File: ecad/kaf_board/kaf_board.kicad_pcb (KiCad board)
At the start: 4 copper layers, 116 x 71 mm, 234 parts, among them J1 Barrel_Jack_Switch, J2 USB_OTG, J3 AUX, J4 Peltier1, J5 Peltier2, M1 Motor_Servo, M2 Servo cut-out, Q1 MMBT3904LT1G, Q2 NTD4804N, Q3 NTD4804N, U1 MAX4649, U10 LM224, U11 LM224, U12 LM224, U13 LD1117S12CTR_SOT223, U14 LD1117S33CTR_SOT223, U15 LTC3265*FE, U16 93LCxxBxxOT, U17 FT2232H, U18 ICE40HX1K-VQ100, U19 W25X20CL, U2 ADP7118AUJZ, U20 MCP3004, U21 TC4427, U3 AD9826, U4 KAF-CDIP24, U5 TL432LIAIDBZR, U6 TL432LIAIDBZR, U7 TC4427, U8 TC4427, U9 TC4428, X1 KC7050A-C3, Y1 12 MHz

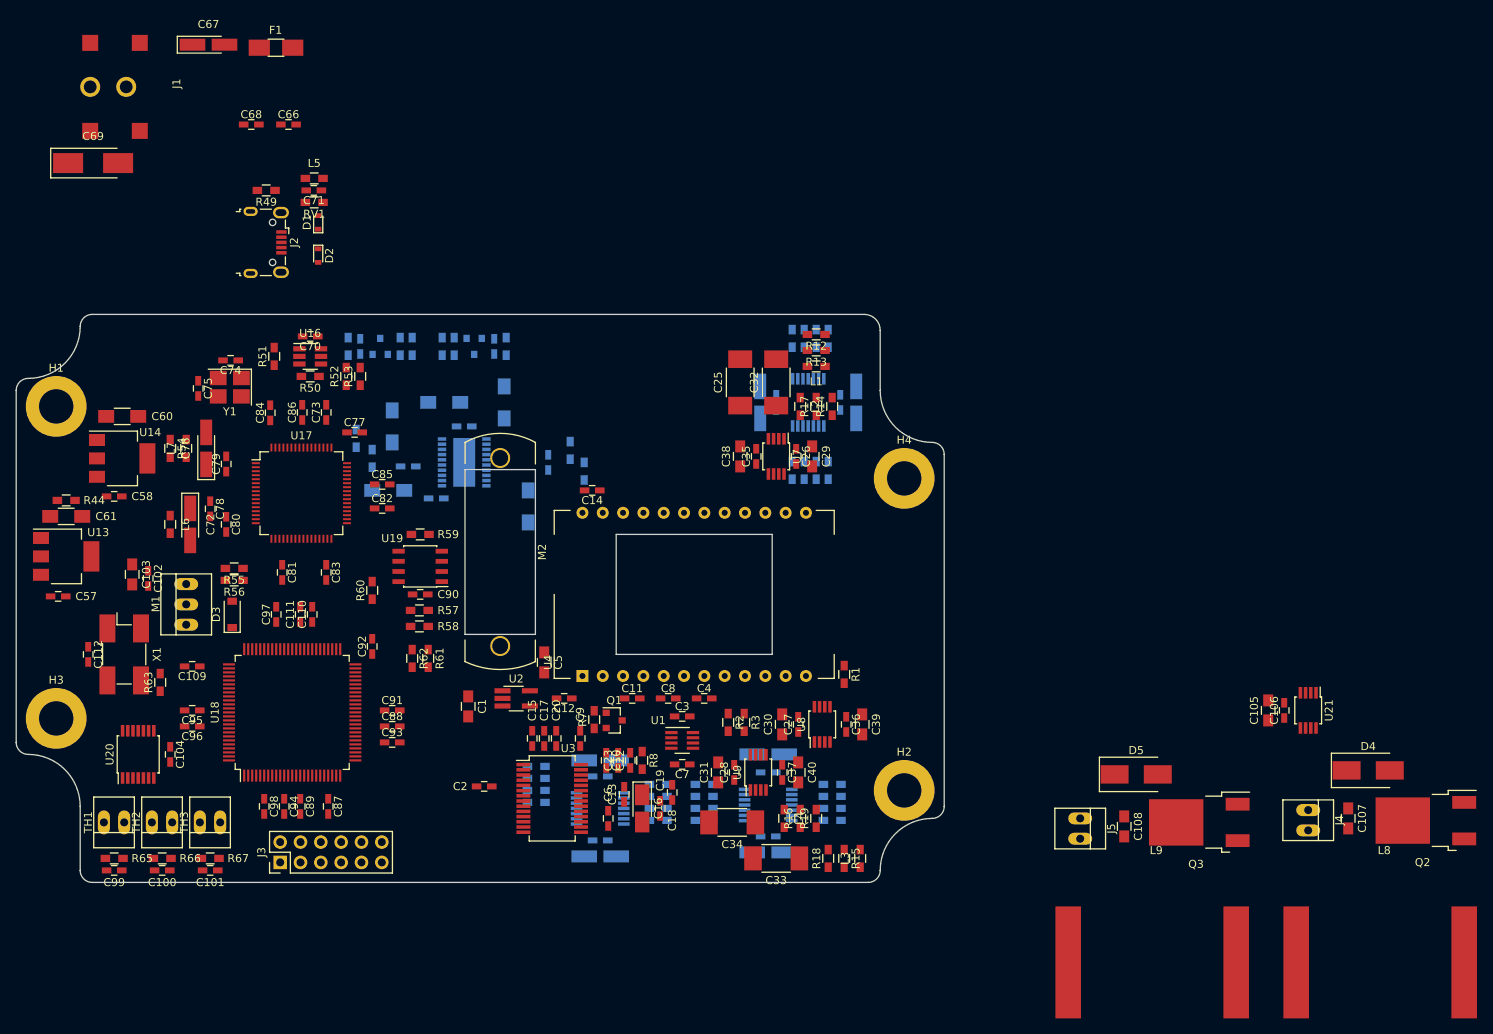
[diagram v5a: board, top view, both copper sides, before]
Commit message: changed all board i/o to go through a pin header and placed power components
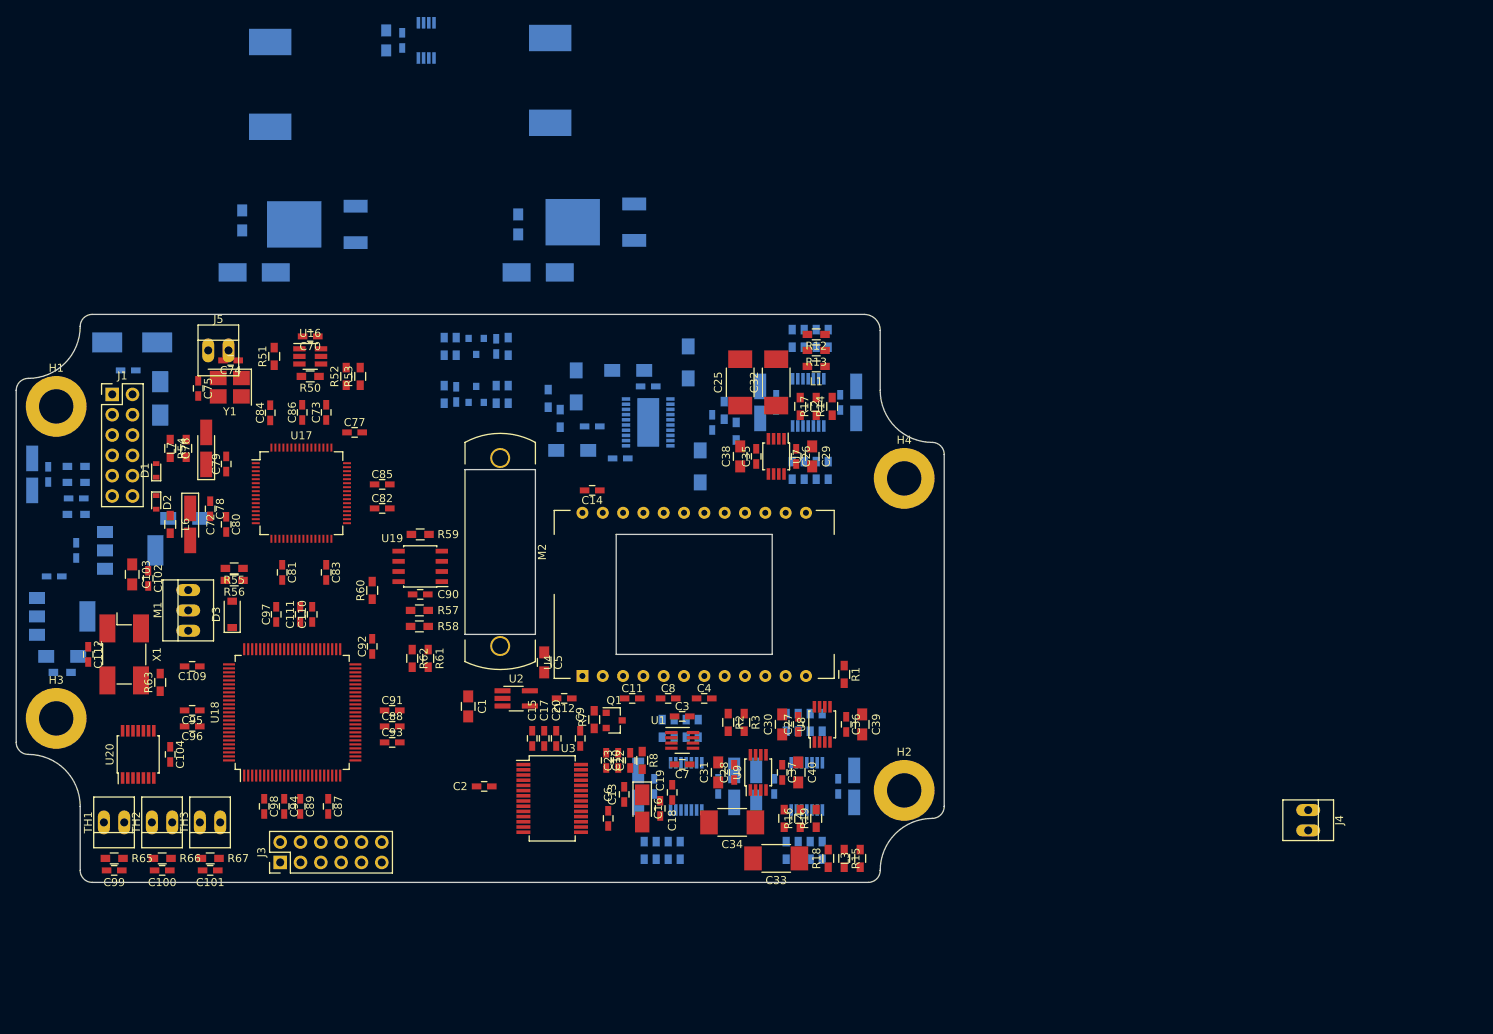
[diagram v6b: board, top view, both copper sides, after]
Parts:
- removed J2: USB_OTG, Connectors_USB:USB_Micro-B_Wuerth-629105150521
- C105, C106, C107, C108, C57, C58, C60, C61, C66, C67, C68, C69, C71, D4, D5, F1, L5, Q2, Q3, R44, R49, RV1, U13, U14, U21: moved to B.Cu
- J1: value Barrel_Jack_Switch -> I/O; footprint kaf_board:Barrel_jack_switched_SMD -> Pin_Headers:Pin_Header_Straight_2x06_Pitch2.54mm
- L8, L9: footprint kaf_board:Murata_L_SMD_19.5x27.0mm -> kaf_board:L_Bourns_1210; moved to B.Cu
- moved L9 155.6 mm to (123.8, 38.2)
- moved L8 151.4 mm to (158.8, 37.8)
- moved C105 138.5 mm to (138.2, 32.8), turned to 270 degrees
- moved C106 138.5 mm to (140.2, 32.8), turned to 270 degrees
- moved U21 138.5 mm to (143.2, 32.8), turned to 90 degrees
- moved C108 133.8 mm to (120.2, 55.2), turned to 90 degrees
- moved Q3 130.7 mm to (134.4, 58.0)
- moved C107 127.6 mm to (154.8, 55.8), turned to 90 degrees
- moved D5 126.9 mm to (121.8, 61.8)
- moved Q2 125.3 mm to (169.2, 57.8)
- moved J5 123.7 mm to (116.0, 71.5), turned to 0 degrees
- moved D4 121.0 mm to (157.2, 61.8)
- moved C67 58.1 mm to (94.0, 87.0), turned to 90 degrees
- moved C66 53.1 mm to (96.0, 87.0), turned to 90 degrees
- moved C71 48.6 mm to (99.5, 90.0), turned to 0 degrees
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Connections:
- C105 pad 1: +12V -> /V_TEC1
- C106 pad 1: +12V -> /V_TEC1
- C107 pad 1: +12V -> /V_TEC1
- C108 pad 1: +12V -> /V_TEC1
- C71 pad 2: /usb-interface/USB_VBUS -> /VUSB
- D1 pad 1: Net-(D1-Pad1) -> /DM
- D2 pad 1: Net-(D2-Pad1) -> /DP
- D4 pad 1: +12V -> /V_TEC1
- D5 pad 1: +12V -> /V_TEC1
- F1 pad 2: Net-(F1-Pad2) -> /V_IN
- J1 pad 1: Net-(F1-Pad2) -> /V_TEC1
- J1 pad 2: GND -> /V_TEC1
- J1 pad 3: (no net) -> GND
- J3 pad 7: /fpga/AUX6 -> /fpga/AUX7
- J4 pad 1: +12V -> /V_TEC1
- J5 pad 1: +12V -> /V_TEC1
- L5 pad 1: /usb-interface/USB_VBUS -> /VUSB
- R55 pad 2: /usb-interface/USB_VBUS -> /VUSB
- RV1 pad 2: /usb-interface/USB_VBUS -> /VUSB
- U1 pad 8: (no net) -> /ccd/V_AMPL
- U10 pad 1: /ccd/V_AMP -> /ccd/V_AMPL
- U10 pad 2: /ccd/V_AMP -> /ccd/V_AMPL
- U17 pad 7: Net-(D1-Pad1) -> /DM
- U17 pad 8: Net-(D2-Pad1) -> /DP
- U18 pad 9: (no net) -> /fpga/AUX7
- U21 pad 6: +12V -> /V_TEC1

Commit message: have made a preliminary placement of components
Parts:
- removed J5: Peltier2, Connectors:PINHEAD1-2
- added J2: TEC1, Connectors:PINHEAD1-2, F.Cu at (104.0, 70.5)
- J4: value Peltier1 -> TEC2
- moved J4 155.4 mm to (109.5, 70.5), turned to 0 degrees
- moved C105 72.3 mm to (121.2, 103.0), turned to 0 degrees
- moved C106 70.8 mm to (121.2, 101.0), turned to 0 degrees
- moved U21 68.9 mm to (121.2, 98.0), turned to 180 degrees
- moved Q2 57.4 mm to (124.0, 93.0)
- moved L8 53.4 mm to (120.0, 74.5)
- moved C107 52.6 mm to (105.2, 73.5), turned to 0 degrees
- moved D4 46.0 mm to (117.2, 84.5)
- moved L9 37.4 mm to (132.8, 74.5)
- moved Q3 35.4 mm to (140.0, 93.0)
- moved D5 24.1 mm to (129.8, 84.5)
- moved R51 22.5 mm to (144.0, 83.0), turned to 180 degrees
- moved C60 21.8 mm to (102.2, 111.5), turned to 180 degrees
- moved C108 20.6 mm to (110.8, 73.5), turned to 0 degrees
- moved C57 20.2 mm to (113.5, 111.0)
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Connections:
- C107 pad 2: /thermo_and_mechanical/- -> Net-(C107-Pad2)
- C108 pad 1: /V_TEC1 -> /V_TEC2
- C108 pad 2: /thermo_and_mechanical/- -> Net-(C108-Pad2)
- D5 pad 1: /V_TEC1 -> /V_TEC2
- J1 pad 2: /V_TEC1 -> /V_TEC2
- J3 pad 11: /fpga/AUX11 -> +3V3
- J3 pad 12: /fpga/AUX12 -> GND
- J4 pad 1: /V_TEC1 -> /V_TEC2
- J4 pad 2: /thermo_and_mechanical/- -> Net-(C108-Pad2)
- L8 pad 1: /thermo_and_mechanical/- -> Net-(C107-Pad2)
- L9 pad 1: /thermo_and_mechanical/- -> Net-(C108-Pad2)
- U18 pad 15: /fpga/AUX11 -> /ccd/AMP_OFF
- U18 pad 16: /fpga/AUX12 -> /ccd/H_3.3V
- U18 pad 18: /ccd/AMP_OFF -> /ccd/R_3.3V
- U18 pad 19: /ccd/H_3.3V -> /ccd/AD_SLOAD
- U18 pad 20: /ccd/R_3.3V -> /ccd/AD_SCLK
- U18 pad 21: /ccd/AD_SLOAD -> /ccd/AD_SDATA
- U18 pad 24: /ccd/AD_SCLK -> /ccd/AD_D0
- U18 pad 25: /ccd/AD_SDATA -> /ccd/AD_D1
- U18 pad 26: /ccd/AD_D0 -> /ccd/AD_D2
- U18 pad 27: /ccd/AD_D1 -> /ccd/AD_D3
- U18 pad 28: /ccd/AD_D2 -> /ccd/AD_D4
- U18 pad 29: /ccd/AD_D3 -> /ccd/AD_D5
- U18 pad 30: /ccd/AD_D4 -> /ccd/AD_D6
- U18 pad 33: /ccd/AD_D5 -> /ccd/AD_D7
- U18 pad 34: /ccd/AD_D6 -> /ccd/AD_OEB
- U18 pad 36: /ccd/AD_D7 -> /ccd/AD_ADCLK
- U18 pad 37: /ccd/AD_OEB -> /ccd/AD_CDSCLK2
- U18 pad 41: /ccd/AD_CDSCLK2 -> /fpga/V1_3.3V
- U18 pad 42: /ccd/AD_ADCLK -> /ccd/V1_3.3V
- U18 pad 78: /fpga/V1_3.3V -> (no net)
- U18 pad 79: /ccd/V1_3.3V -> (no net)
- U18 pad 99: GND -> /fpga/PWM_TEC2
- U21 pad 4: GND -> /fpga/PWM_TEC2

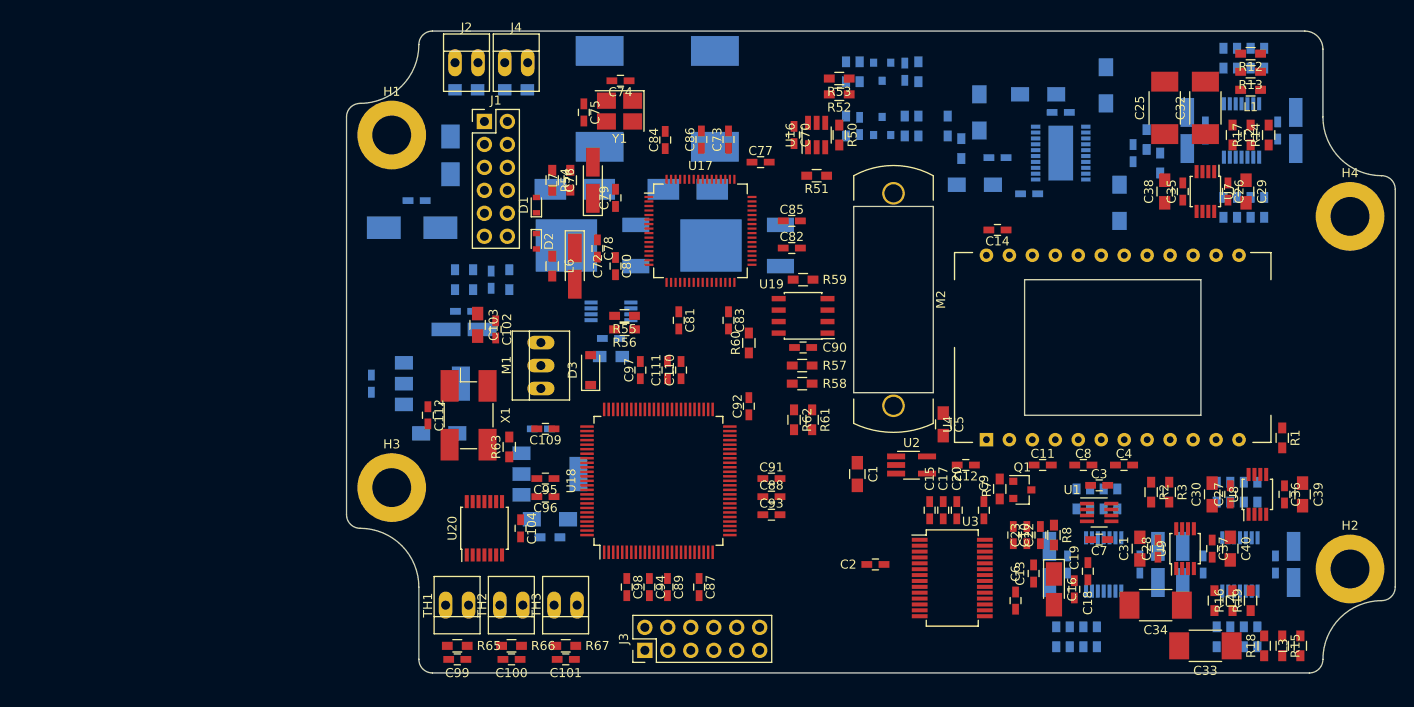
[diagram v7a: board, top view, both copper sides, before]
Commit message: changed some connectors and moved components
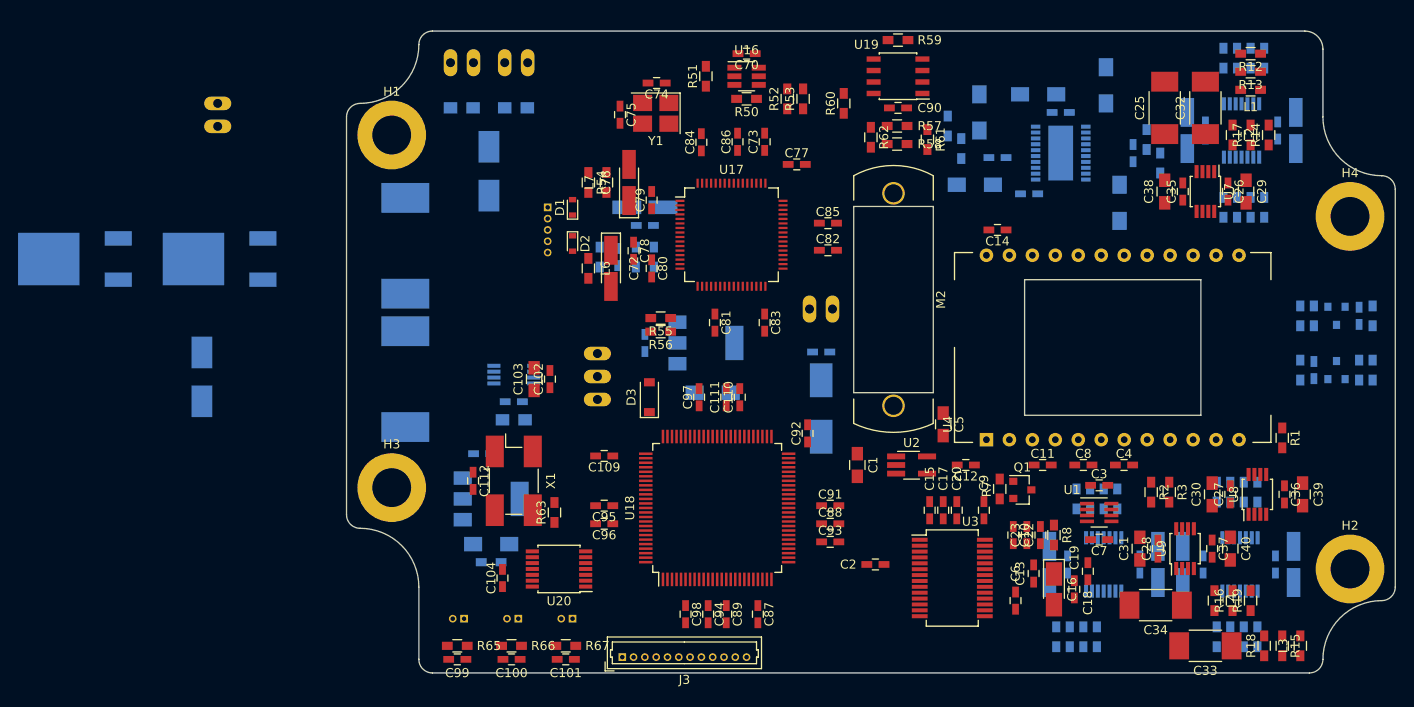
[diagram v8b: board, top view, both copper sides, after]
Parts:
- removed F1: Fuse, Fuse_Holders_and_Fuses:Fuse_SMD1206_HandSoldering
- added J5: USB, Connectors_Molex:Molex_PicoBlade_53047-0510_05x1.25mm_Straight, B.Cu at (114.2, 86.5)
- added J6: TECPWR, Connectors:PINHEAD1-2, B.Cu at (77.8, 75.0)
- J1: value I/O -> PWR; footprint Pin_Headers:Pin_Header_Straight_2x06_Pitch2.54mm -> Connectors:PINHEAD1-2; moved to B.Cu
- J2, J4, M1: moved to B.Cu
- J3: value AUX -> Conn_01x12; footprint Pin_Headers:Pin_Header_Straight_2x06_Pitch2.54mm -> Connectors_Molex:Molex_PicoBlade_53047-1210_12x1.25mm_Straight
- TH1, TH2, TH3: footprint Connectors:PINHEAD1-2 -> Connectors_Molex:Molex_PicoBlade_53047-0210_02x1.25mm_Straight; moved to B.Cu
- U17: value FT2232H -> FT2232HL
- moved D5 57.6 mm to (76.0, 105.2), turned to 90 degrees
- moved Q2 57.3 mm to (66.8, 94.5)
- moved Q3 57.3 mm to (82.8, 94.5)
- moved C21 57.0 mm to (204.0, 98.5)
- moved C24 57.0 mm to (199.0, 104.5)
- moved R10 57.0 mm to (204.0, 104.5)
- moved R11 57.0 mm to (205.5, 104.5)
- moved R4 57.0 mm to (205.5, 98.5)
- moved R5 57.0 mm to (199.0, 98.5)
- moved R6 57.0 mm to (197.5, 98.5)
- moved R9 57.0 mm to (197.5, 104.5)
- moved U5 57.0 mm to (201.5, 98.5)
- moved U6 57.0 mm to (201.5, 104.5)
- moved C69 49.5 mm to (144.5, 108.8), turned to 270 degrees
- moved C68 47.8 mm to (144.5, 102.5)
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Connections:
- C1 pad 1: GNDA -> GND
- C105 pad 1: /V_TEC1 -> /thermo_and_mechanical/V_TEC
- C106 pad 1: /V_TEC1 -> /thermo_and_mechanical/V_TEC
- C107 pad 1: /V_TEC1 -> /thermo_and_mechanical/V_TEC
- C108 pad 1: /V_TEC2 -> /thermo_and_mechanical/V_TEC
- C11 pad 2: GNDA -> GND
- C12 pad 2: GNDA -> GND
- C14 pad 2: GNDA -> GND
- C15 pad 2: GNDA -> GND
- C17 pad 1: GNDA -> GND
- C18 pad 2: GNDA -> GND
- C19 pad 2: GNDA -> GND
- C2 pad 1: GNDA -> GND
- C20 pad 1: GNDA -> GND
- C21 pad 2: GNDA -> GND
- C22 pad 1: GNDA -> GND
- C23 pad 1: GNDA -> GND
- C24 pad 1: GNDA -> GND
- C26 pad 1: GNDA -> GND
- C27 pad 1: GNDA -> GND
- C28 pad 1: GNDA -> GND
- C29 pad 1: GNDA -> GND
- C3 pad 1: GNDA -> GND
- C30 pad 1: GNDA -> GND
- C31 pad 1: GNDA -> GND
- C35 pad 1: GNDA -> GND
- C36 pad 1: GNDA -> GND
- C37 pad 1: GNDA -> GND
- C38 pad 1: GNDA -> GND
- C39 pad 1: GNDA -> GND
- C4 pad 2: GNDA -> GND
- C40 pad 1: GNDA -> GND
- C41 pad 1: GNDA -> GND
- C42 pad 1: GNDA -> GND
- C43 pad 2: GNDA -> GND
- C44 pad 1: GNDA -> GND
- C45 pad 1: GNDA -> GND
- C46 pad 1: GNDA -> GND
- C47 pad 2: GNDA -> GND
- C48 pad 1: GNDA -> GND
- C49 pad 1: GNDA -> GND
- C5 pad 1: GNDA -> GND
- C50 pad 1: GNDA -> GND
- C51 pad 2: GNDA -> GND
- C52 pad 1: GNDA -> GND
- C53 pad 2: GNDA -> GND
- C54 pad 2: GNDA -> GND
- C56 pad 2: GNDA -> GND
- C6 pad 1: GNDA -> GND
- C62 pad 2: GNDA -> GND
- C63 pad 2: GNDA -> GND
- C64 pad 2: GNDA -> GND
- C65 pad 1: GNDA -> GND
- C7 pad 1: GNDA -> GND
- C71 pad 2: /VUSB -> /usb-interface/VUSB
- C8 pad 2: GNDA -> GND
- C9 pad 1: GNDA -> GND
- D1 pad 1: /DM -> /usb-interface/DM
- D2 pad 1: /DP -> /usb-interface/DP
- D4 pad 1: /V_TEC1 -> /thermo_and_mechanical/V_TEC
- D5 pad 1: /V_TEC2 -> /thermo_and_mechanical/V_TEC
- J1 pad 1: /V_TEC1 -> +12V
- J1 pad 2: /V_TEC2 -> GND
- J2 pad 1: /V_TEC1 -> /thermo_and_mechanical/V_TEC
- J3 pad 11: +3V3 -> GND
- J3 pad 12: GND -> +3V3
- J4 pad 1: /V_TEC2 -> /thermo_and_mechanical/V_TEC
- L5 pad 1: /VUSB -> /usb-interface/VUSB
- R11 pad 1: GNDA -> GND
- R46 pad 2: GNDA -> GND
- R47 pad 1: GNDA -> GND
- R5 pad 1: GNDA -> GND
- R55 pad 2: /VUSB -> (no net)
- R8 pad 2: GNDA -> GND
- RV1 pad 2: /VUSB -> /usb-interface/VUSB
- U1 pad 3: GNDA -> GND
- U15 pad 14: GNDA -> GND
- U15 pad 16: GNDA -> GND
- U15 pad 21: GNDA -> GND
- U17 pad 7: /DM -> /usb-interface/DM
- U17 pad 8: /DP -> /usb-interface/DP
- U2 pad 2: GNDA -> GND
- U21 pad 6: /V_TEC1 -> /thermo_and_mechanical/V_TEC
- U3 pad 19: GNDA -> GND
- U3 pad 22: GNDA -> GND
- U3 pad 24: GNDA -> GND
- U3 pad 27: GNDA -> GND
- U3 pad 6: GNDA -> GND
- U4 pad 12: GNDA -> GND
- U4 pad 13: GNDA -> GND
- U4 pad 14: GNDA -> GND
- U5 pad 2: GNDA -> GND
- U6 pad 3: GNDA -> GND
- U9 pad 5: /ccd/H2 -> /ccd/H1
- U9 pad 7: /ccd/H1 -> /ccd/H2
